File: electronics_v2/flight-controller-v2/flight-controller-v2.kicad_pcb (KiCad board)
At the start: 2 copper layers, 45 x 84 mm, 91 parts, among them J1 Conn_02x05_Odd_Even, J2 USB_B_Micro, J3 Conn_02x03_Odd_Even, J4 Conn_01x05, J5 Conn_01x06, J6 Conn_01x05, SW1 SW_Push, SW2 SW_Push, U1 LM1117-3.3, U2 STM32F411RETx, U3 ESP-12E, U4 CS49E, U5 LM393, U6 MPU-6050, U7 HMC5883L, U8 BMP280, Y1 8MHz

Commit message: update silkscreen and add tag for order number
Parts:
- moved JP1 1.50 mm to (155.0, 98.2)
- moved JP2 1.50 mm to (155.0, 95.5)
- moved JP3 1.50 mm to (155.0, 92.5)
- moved JP4 1.50 mm to (155.0, 89.8)
- moved JP5 1.50 mm to (155.0, 87.0)
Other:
- board text added: "GPIO0"
- board text added: "GPIO12"
- board text added: "GPIO2"
- board text added: "JLCJLCJLCJLC"
- board text added: "RXD0"
- board text added: "TXD0"
- board text removed: "MRX"
- board text removed: "MTX"
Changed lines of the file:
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@@
   )
   (footprint "Jumper:SolderJumper-2_P1.3mm_Open_TrianglePad1.0x1.5mm" (layer "B.Cu")
-    (at 156.5 95.5)
+    (at 155 95.5)
     (descr "SMD Solder Jumper, 1x1.5mm Triangular Pads, 0.3mm gap, open")
     (tags "solder jumper open")
@@
   )
   (footprint "Jumper:SolderJumper-2_P1.3mm_Open_TrianglePad1.0x1.5mm" (layer "B.Cu")
-    (at 156.5 87)
+    (at 155 87)
     (descr "SMD Solder Jumper, 1x1.5mm Triangular Pads, 0.3mm gap, open")
     (tags "solder jumper open")
@@
   )
   (footprint "Jumper:SolderJumper-2_P1.3mm_Open_TrianglePad1.0x1.5mm" (layer "B.Cu")
-    (at 156.5 89.75)
+    (at 155 89.75)
     (descr "SMD Solder Jumper, 1x1.5mm Triangular Pads, 0.3mm gap, open")
     (tags "solder jumper open")
@@
   )
   (footprint "Jumper:SolderJumper-2_P1.3mm_Open_TrianglePad1.0x1.5mm" (layer "B.Cu")
-    (at 156.5 92.5)
+    (at 155 92.5)
     (descr "SMD Solder Jumper, 1x1.5mm Triangular Pads, 0.3mm gap, open")
     (tags "solder jumper open")
@@
   )
   (footprint "Jumper:SolderJumper-2_P1.3mm_Open_TrianglePad1.0x1.5mm" (layer "B.Cu")
-    (at 156.5 98.25)
+    (at 155 98.25)
     (descr "SMD Solder Jumper, 1x1.5mm Triangular Pads, 0.3mm gap, open")
     (tags "solder jumper open")
@@
   (gr_arc (start 161.000001 85) (mid 161.292894 84.292894) (end 162 84.000001) (layer "Edge.Cuts") (width 0.1))
   (gr_arc (start 124 80) (mid 125.171573 77.171573) (end 128 76) (layer "Edge.Cuts") (width 0.1))
-  (gr_text "RST" (at 154.5 87) (layer "B.SilkS")
-    (effects (font (size 0.75 0.75) (thickness 0.15)) (justify left mirror))
+  (gr_text "RST" (at 156.75 87) (layer "B.SilkS")
+    (effects (font (size 0.75 0.75) (thickness 0.15)) (justify right mirror))
   )
-  (gr_text "UAV TVC Goose\nFlight Controller V2.0\nby Eryk Możdżeń\nJuly 2023" (at 158 81) (layer "B.SilkS")
+  (gr_text "UAV TVC Goose\nFlight Controller V2.0\nby Eryk Możdżeń\nJuly 2023" (at 156.75 81) (layer "B.SilkS")
     (effects (font (size 1 1) (thickness 0.15)) (justify left mirror))
   )
-  (gr_text "MRX" (at 154.5 98.25) (layer "B.SilkS")
+  (gr_text "GPIO0" (at 153.25 92.5) (layer "B.SilkS")
+    (effects (font (size 0.75 0.75) (thickness 0.15)) (justify left mirror))
+  )
+  (gr_text "RX" (at 156.75 98.25) (layer "B.SilkS")
+    (effects (font (size 0.75 0.75) (thickness 0.15)) (justify right mirror))
+  )
+  (gr_text "GPIO12" (at 153.25 87) (layer "B.SilkS")
     (effects (font (size 0.75 0.75) (thickness 0.15)) (justify left mirror))
   )
-  (gr_text "MTX" (at 154.5 95.5) (layer "B.SilkS")
+  (gr_text "TX" (at 156.75 95.5) (layer "B.SilkS")
+    (effects (font (size 0.75 0.75) (thickness 0.15)) (justify right mirror))
+  )
+  (gr_text "GPIO2" (at 153.25 89.75) (layer "B.SilkS")
     (effects (font (size 0.75 0.75) (thickness 0.15)) (justify left mirror))
   )
-  (gr_text "SWDIO" (at 154.5 92.5) (layer "B.SilkS")
+  (gr_text "SWDIO" (at 156.75 92.5) (layer "B.SilkS")
+    (effects (font (size 0.75 0.75) (thickness 0.15)) (justify right mirror))
+  )
+  (gr_text "TXD0" (at 153.25 98.25) (layer "B.SilkS")
     (effects (font (size 0.75 0.75) (thickness 0.15)) (justify left mirror))
   )
-  (gr_text "SWCLK" (at 154.5 89.75) (layer "B.SilkS")
+  (gr_text "SWCLK" (at 156.75 89.75) (layer "B.SilkS")
+    (effects (font (size 0.75 0.75) (thickness 0.15)) (justify right mirror))
+  )
+  (gr_text "RXD0" (at 153.25 95.5) (layer "B.SilkS")
     (effects (font (size 0.75 0.75) (thickness 0.15)) (justify left mirror))
   )
@@
     (effects (font (size 0.75 0.75) (thickness 0.15)))
   )
+  (gr_text "JLCJLCJLCJLC" (at 159 92.5 90) (layer "F.SilkS")
+    (effects (font (size 1 1) (thickness 0.2)))
+  )
   (gr_text "3V3" (at 165.75 113.5) (layer "F.SilkS")

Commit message: edge XT60 connector & INA226 I2C measurement
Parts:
- removed the C1 at (140.9, 110.0)
- removed the C6 at (140.9, 108.0)
- removed the D1 at (136.9, 113.0)
- removed the D2 at (136.9, 105.0)
- removed the J3 at (142.0, 143.7)
- removed the R1 at (137.4, 110.0)
- removed the R2 at (140.9, 112.0)
- removed the R3 at (137.4, 108.0)
- removed the R4 at (140.9, 106.0)
- added J6: Conn_02x03_Odd_Even, Connector_IDC:IDC-Header_2x03_P2.54mm_Vertical, F.Cu at (137.5, 146.5)
- moved R4 1.52 mm to (150.0, 140.0)
- moved R8 1.52 mm to (150.0, 142.0)
- moved G*** 0.50 mm to (155.1, 145.3)
- renumbered C2 to C1, C8 to C10, C9 to C11, C14 to C12, C10 to C13, C15 to C14, C11 to C15, C12 to C16, C7 to C17, C19 to C18, C26 to C19, C3 to C2, C27 to C20, C23 to C21, C24 to C22, C30 to C23, C31 to C24, C29 to C25, C25 to C26, C22 to C27, C4 to C3, C5 to C4, C20 to C5, C13 to C6, C21 to C7, C16 to C8, C17 to C9, D3 to D1, D4 to D2, D5 to D3, D6 to D4, J5 to J3, J6 to J5, R6 to R1, R15 to R10, R10 to R11, R9 to R12, R16 to R13, R11 to R14, R12 to R15, R23 to R16, R25 to R17, R24 to R18, R20 to R19, R5 to R2, R21 to R20, R22 to R21, R7 to R3, R13 to R4, R17 to R5, R18 to R6, R19 to R7, R14 to R9, U8 to U4, U4 to U5, U5 to U7, U7 to U8
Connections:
- net /sensors/I2C_SCL renamed /sensors/INT_I2C_SCL
- net /sensors/I2C_SDA renamed /sensors/INT_I2C_SDA
- J1 pad 10: /power/BATT_V_SENSE -> /power/EXT_I2C_SCL
- J1 pad 8: /power/BATT_I_SENSE -> /power/EXT_I2C_SDA
- R4 pad 2: /ucontroller/VLX_I2C3_SDA -> /power/EXT_I2C_SDA
- R8 pad 2: /ucontroller/VLX_I2C3_SCL -> /power/EXT_I2C_SCL
- U2 pad 24: /power/I_FILTER -> unconnected-(U2-Pad24)
- U2 pad 25: /power/V_FILTER -> unconnected-(U2-Pad25)
- U2 pad 40: /ucontroller/VLX_I2C3_SDA -> /power/EXT_I2C_SDA
- U2 pad 41: /ucontroller/VLX_I2C3_SCL -> /power/EXT_I2C_SCL
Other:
- board text removed: "ISENS"
- board text removed: "VSENS"

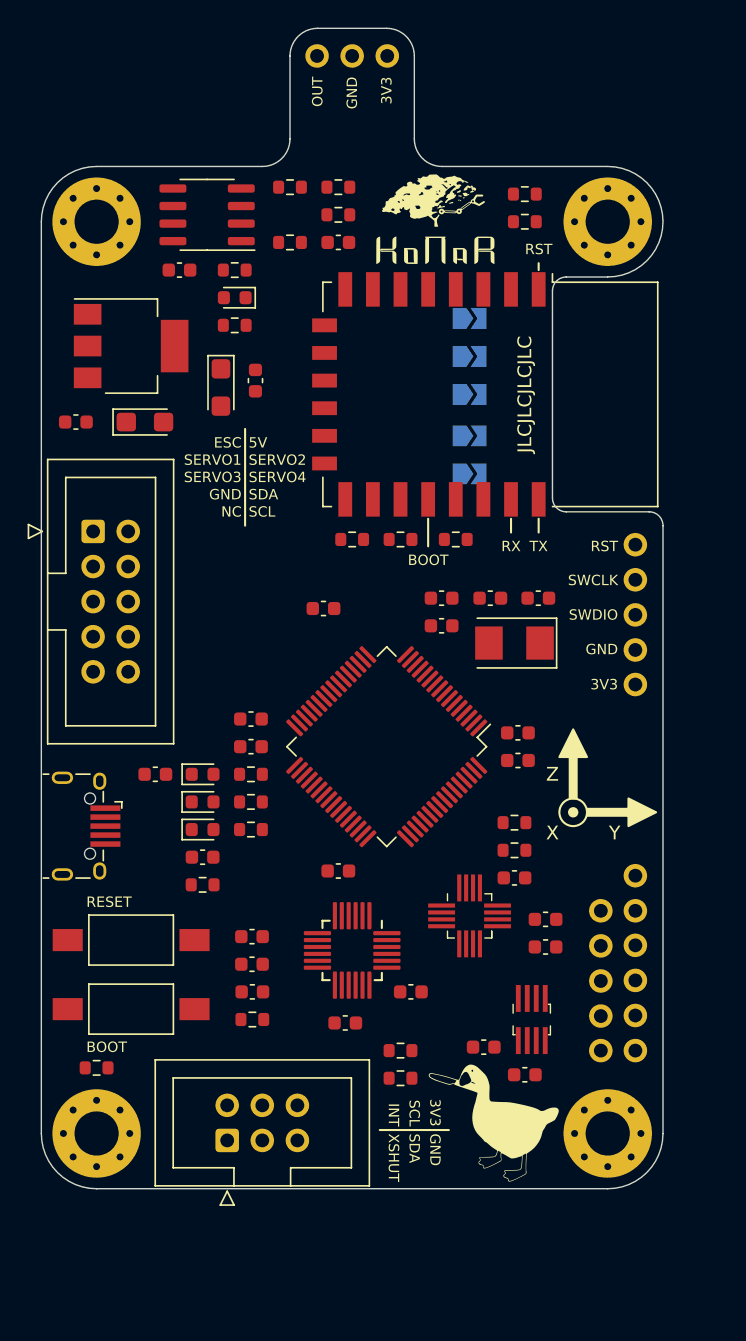
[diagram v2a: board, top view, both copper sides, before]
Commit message: move PLI to FC
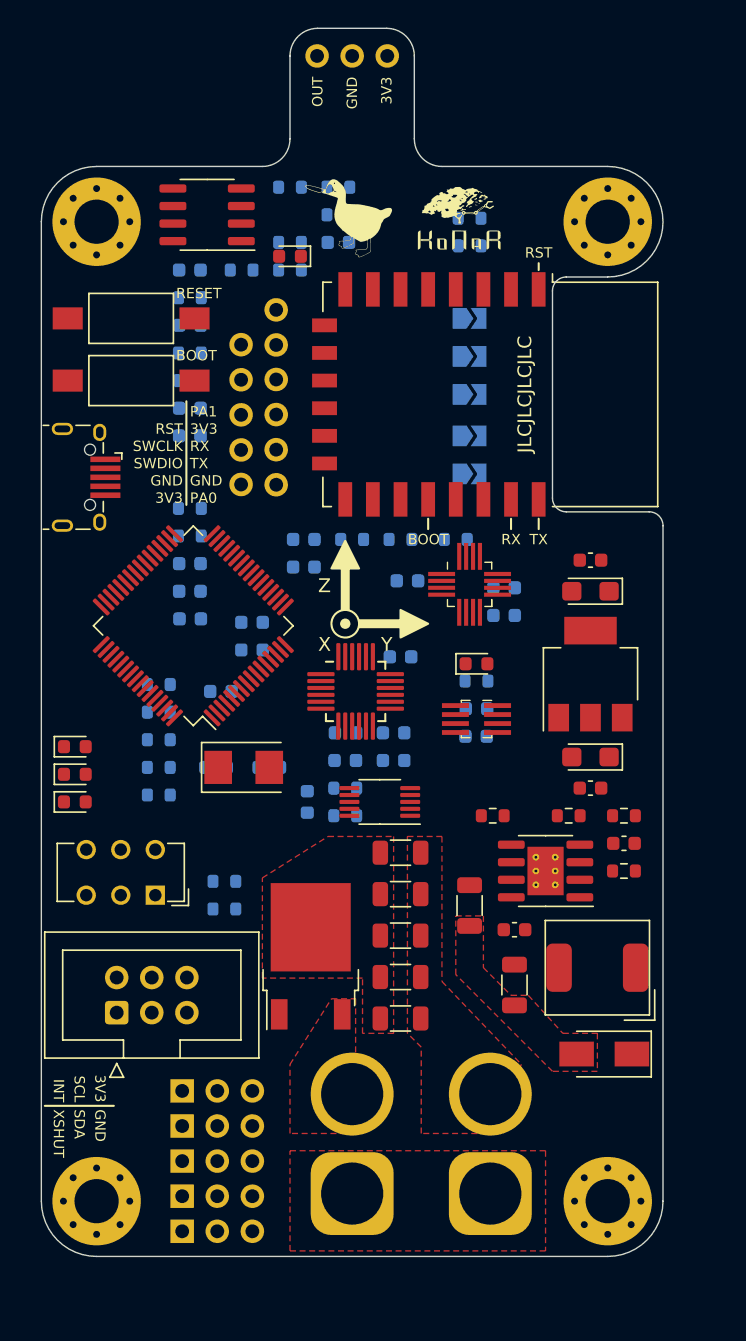
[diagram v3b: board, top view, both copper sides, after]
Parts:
- removed the G*** at (152.5, 80.5)
- removed the G*** at (155.1, 145.3)
- removed the G*** at (146.6, 108.2)
- added C10: 100n, Capacitor_SMD:C_0603_1608Metric, B.Cu at (146.0, 119.0)
- added C5: 10u/50V, Capacitor_SMD:C_1206_3216Metric, F.Cu at (155.0, 129.5)
- added C6: 100n, Capacitor_SMD:C_0603_1608Metric, F.Cu at (158.2, 131.2)
- added C7: 150p, Capacitor_SMD:C_0603_1608Metric, F.Cu at (166.2, 125.0)
- added C8: 22u/25V, Capacitor_SMD:C_1206_3216Metric, F.Cu at (158.2, 135.2)
- added C9: 100n, Capacitor_SMD:C_0603_1608Metric, B.Cu at (143.2, 122.0)
- added D1: RED, LED_SMD:LED_0603_1608Metric, F.Cu at (155.5, 112.0)
- added D2: SS34, Diode_SMD:D_SMA, F.Cu at (164.8, 140.2)
- added G***: LOGO, LOGO, F.Cu at (154.2, 80.2)
- added G***: LOGO, LOGO, F.Cu at (145.1, 79.8)
- added J2: Conn_01x03, Connector_PinHeader_2.54mm:PinHeader_1x03_P2.54mm_Vertical, B.Cu at (134.2, 153.1)
- added J3: Conn_01x03, Connector_PinHeader_2.54mm:PinHeader_1x03_P2.54mm_Vertical, B.Cu at (134.2, 150.5)
- added J4: Conn_01x03, Connector_PinHeader_2.54mm:PinHeader_1x03_P2.54mm_Vertical, B.Cu at (134.2, 148.0)
- added J6: Conn_01x03, Connector_PinHeader_2.54mm:PinHeader_1x03_P2.54mm_Vertical, B.Cu at (134.2, 142.9)
- added J7: Conn_01x02, Connector_AMASS:AMASS_XT60-F_1x02_P7.20mm_Vertical, B.Cu at (156.5, 150.3)
- added L1: 22u, Inductor_SMD:L_AVX_LMLP07A7, F.Cu at (164.2, 134.0)
- added Q1: IRFR5305, Package_TO_SOT_SMD:TO-252-2, F.Cu at (143.5, 133.2)
- added R1: 10k, Resistor_SMD:R_0603_1608Metric, B.Cu at (137.2, 129.8)
- added R10: 10m, Resistor_SMD:R_1206_3216Metric, F.Cu at (150.0, 137.7)
- added R11: 10, Resistor_SMD:R_0603_1608Metric, B.Cu at (146.0, 123.0)
- added R12: 10, Resistor_SMD:R_0603_1608Metric, B.Cu at (146.0, 121.0)
- added R13: 210k, Resistor_SMD:R_0603_1608Metric, F.Cu at (166.2, 123.0)
- added R14: 39k, Resistor_SMD:R_0603_1608Metric, F.Cu at (162.2, 123.0)
- added R2: 1k, Resistor_SMD:R_0603_1608Metric, B.Cu at (137.2, 127.8)
- added R3: 100k, Resistor_SMD:R_0603_1608Metric, F.Cu at (156.7, 123.0)
- added R4: 1k, Resistor_SMD:R_0603_1608Metric, B.Cu at (155.5, 113.2)
- added R5: 10m, Resistor_SMD:R_1206_3216Metric, F.Cu at (150.0, 125.7)
- added R6: 10m, Resistor_SMD:R_1206_3216Metric, F.Cu at (150.0, 128.7)
- added R7: 10m, Resistor_SMD:R_1206_3216Metric, F.Cu at (150.0, 131.7)
- added R8: 10m, Resistor_SMD:R_1206_3216Metric, F.Cu at (150.0, 134.7)
- added R9: 100k, Resistor_SMD:R_0603_1608Metric, F.Cu at (166.2, 127.0)
- added SW1: SW_Push_SPDT, Button_Switch_THT:SW_CuK_JS202011CQN_DPDT_Straight, F.Cu at (132.2, 128.8)
- added U2: MP1584, Package_SO:SOIC-8-1EP_3.9x4.9mm_P1.27mm_EP2.62x3.51mm_ThermalVias, F.Cu at (160.5, 127.0)
- added U3: INA226, Package_SO:VSSOP-10_3x3mm_P0.5mm, F.Cu at (148.5, 122.0)
- C11: renamed from C5; moved to B.Cu
- C12: renamed from C6; moved to B.Cu
- C13: renamed from C7; moved to B.Cu
- C14: renamed from C8; moved to B.Cu
- C15: renamed from C9; moved to B.Cu
- C16: renamed from C10; moved to B.Cu
- C17: renamed from C11; moved to B.Cu
- C18: renamed from C12; moved to B.Cu
- C19: renamed from C13; moved to B.Cu
- C20: renamed from C14; moved to B.Cu
- C21: renamed from C15; moved to B.Cu
- C22: renamed from C16; moved to B.Cu
- C23: renamed from C17; moved to B.Cu
- C24: renamed from C18; moved to B.Cu
- C25: renamed from C19; moved to B.Cu
- C26: renamed from C20; moved to B.Cu
- C27: renamed from C21; moved to B.Cu
- C28: renamed from C22; moved to B.Cu
- C29: renamed from C23; moved to B.Cu
- C30: renamed from C24; moved to B.Cu
- C31: renamed from C25; moved to B.Cu
- C32: renamed from C26; moved to B.Cu
- C33: renamed from C27; moved to B.Cu
- C34: renamed from C28; moved to B.Cu
- J1: value Conn_02x05_Odd_Even -> Conn_01x02; footprint Connector_IDC:IDC-Header_2x05_P2.54mm_Vertical -> Connector_AMASS:AMASS_XT60-M_1x02_P7.20mm_Vertical; moved to B.Cu
- J5: value Conn_01x05 -> Conn_01x03; footprint goose:tht_pin_01x05 -> Connector_PinHeader_2.54mm:PinHeader_1x03_P2.54mm_Vertical; moved to B.Cu
- R15: renamed from R1; moved to B.Cu
- R16: renamed from R2; moved to B.Cu
- R17: renamed from R3; moved to B.Cu
- R18: renamed from R4; moved to B.Cu
- R19: renamed from R5; moved to B.Cu
- R20: renamed from R6; moved to B.Cu
- R21: renamed from R7; moved to B.Cu
- R22: renamed from R8; moved to B.Cu
- R23: renamed from R9; moved to B.Cu
- R24: renamed from R10; moved to B.Cu
- R25: renamed from R11; moved to B.Cu
- R26: renamed from R12; moved to B.Cu
- R27: renamed from R13; moved to B.Cu
- R28: renamed from R14; moved to B.Cu
- R29: renamed from R15; moved to B.Cu
- R30: renamed from R16; moved to B.Cu
- R31: renamed from R17; moved to B.Cu
- R32: renamed from R18; moved to B.Cu
- R33: renamed from R19; moved to B.Cu
- R34: renamed from R20; moved to B.Cu
- R35: renamed from R21; moved to B.Cu
- moved R15 52.2 mm to (134.8, 89.5)
- moved J1 51.5 mm to (146.5, 150.3), turned to 90 degrees
- moved J9 48.5 mm to (141.0, 86.4)
- moved R17 46.5 mm to (134.8, 91.5), turned to 0 degrees
- moved C1 45.7 mm to (163.8, 121.0)
- moved SW3 45.5 mm to (130.5, 91.5)
- moved SW2 45.0 mm to (130.5, 87.0)
- moved R16 42.5 mm to (134.8, 85.5)
- moved C14 42.5 mm to (134.8, 93.5), turned to 180 degrees
- moved R18 42.1 mm to (134.8, 100.8)
- moved R22 42.1 mm to (134.8, 102.8)
- moved U1 40.9 mm to (163.8, 112.8), turned to 90 degrees
- moved C2 40.4 mm to (163.8, 118.8), turned to 180 degrees
- moved C12 38.5 mm to (134.8, 87.5)
- moved J10 32.0 mm to (138.5, 99.0)
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- renumbered D1 to D3, D2 to D4, D3 to D5, D4 to D6, J4 to J10, J6 to J11, J2 to J8, J3 to J9, SW1 to SW2, SW2 to SW3, U8 to U10, U2 to U4, U3 to U5, U4 to U6, U5 to U7, U6 to U8, U7 to U9
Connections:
- net /sensors/INT_I2C_SCL renamed /power/INT_I2C_SCL
- net /sensors/INT_I2C_SDA renamed /power/INT_I2C_SDA
- J1 pad 1: /power/PWM_THROTTLE -> GND
- J1 pad 2: +5V -> /power/BATTERY_IN
- J11 pad 3: /power/EXT_I2C_SDA -> /sensors/EXT_I2C3_SDA
- J11 pad 4: /power/EXT_I2C_SCL -> /sensors/EXT_I2C3_SCL
- J5 pad 1: /ucontroller/SPI3_MISO -> /power/PWM_SERVO4
- J5 pad 2: /ucontroller/SPI3_MOSI -> +5V
- J5 pad 3: /ucontroller/SPI3_SCK -> GND
- R18 pad 2: /power/EXT_I2C_SDA -> /ucontroller/EXT_I2C3_SDA
- R22 pad 2: /power/EXT_I2C_SCL -> /ucontroller/EXT_I2C3_SCL
- U4 pad 40: /power/EXT_I2C_SDA -> /ucontroller/EXT_I2C3_SDA
- U4 pad 41: /power/EXT_I2C_SCL -> /ucontroller/EXT_I2C3_SCL
- U4 pad 42: /power/PWM_THROTTLE -> /power/PWM_ESC
- U4 pad 51: /ucontroller/SPI3_SCK -> unconnected-(U4-Pad51)
- U4 pad 52: /ucontroller/SPI3_MISO -> unconnected-(U4-Pad52)
- U4 pad 53: /ucontroller/SPI3_MOSI -> unconnected-(U4-Pad53)
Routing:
- added copper zone on F.Cu, net /power/BATTERY_IN
- added copper zone on F.Cu, net /power/SUPPLY
- added copper zone on F.Cu, net GND
- added copper zone on F.Cu, net VBUS
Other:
- board size 45 x 84 mm -> 45 x 88.9 mm
- board text added: "PA0"
- board text added: "PA1"
- board text added: "PWM"
- board text added: "S1"
- board text added: "S2"
- board text added: "S3"
- board text added: "S4"
- board text removed: "NC"
- board text removed: "SERVO1"
- board text removed: "SERVO2"
- board text removed: "SERVO3"
- board text removed: "SERVO4"

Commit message: movemounting hole by 0.1mm
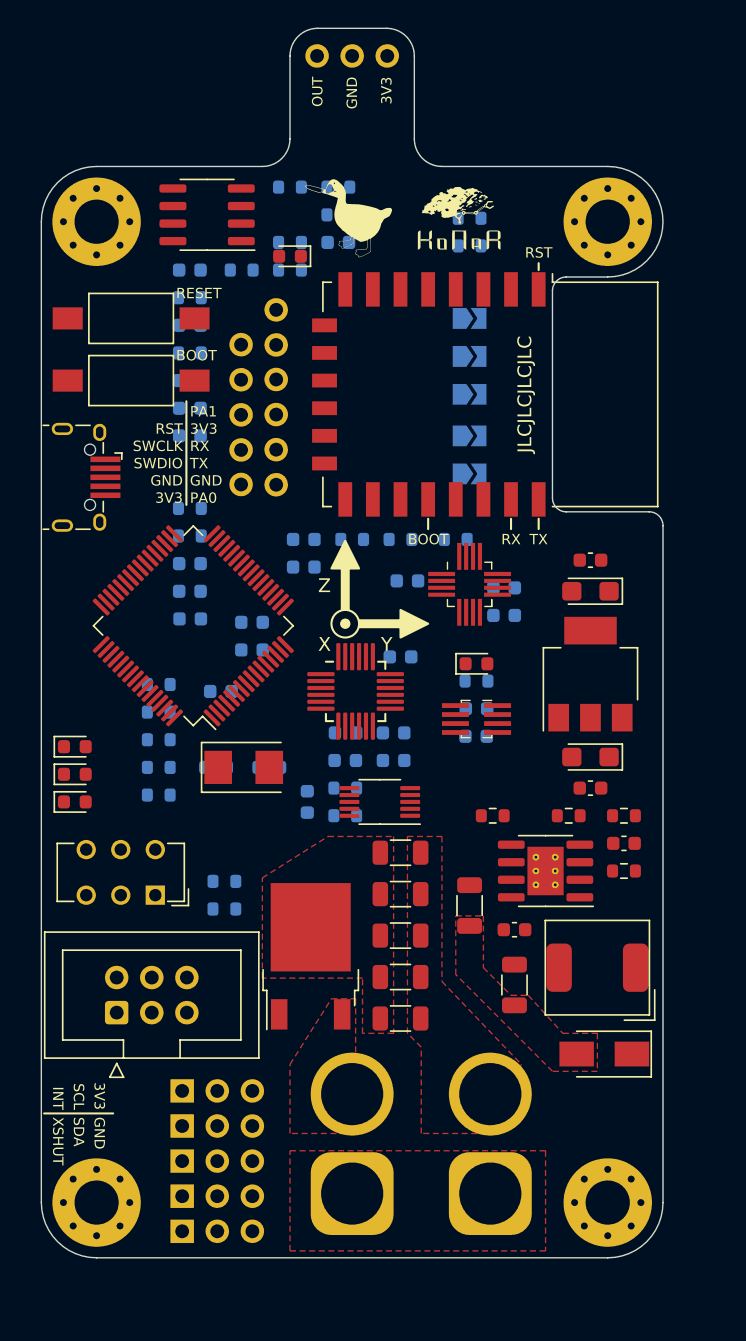
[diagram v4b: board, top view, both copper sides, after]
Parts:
- moved H3 0.10 mm to (128.0, 151.0)
- moved H4 0.10 mm to (165.0, 151.0)
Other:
- board size 45 x 88.9 mm -> 45 x 89 mm

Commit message: fix route names
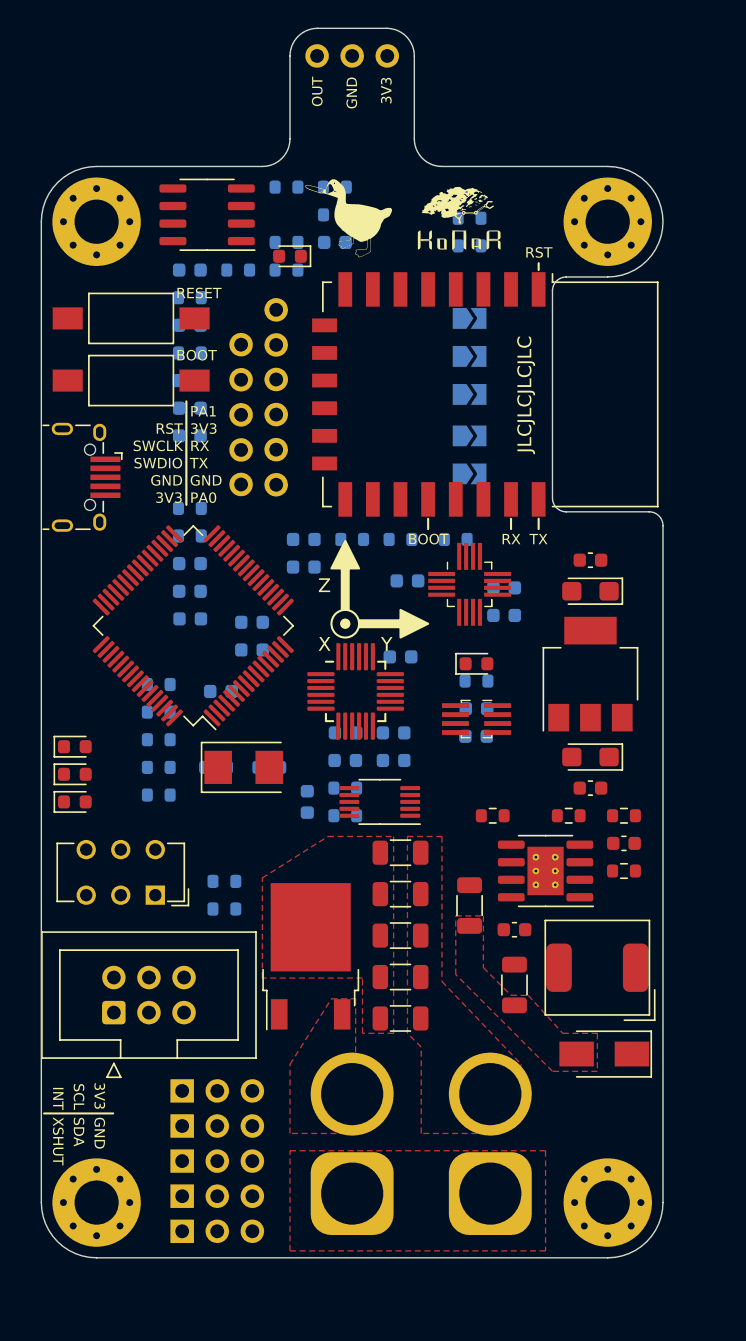
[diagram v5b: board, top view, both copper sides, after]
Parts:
- removed J11: Conn_02x03_Odd_Even, Connector_IDC:IDC-Header_2x03_P2.54mm_Vertical
- added J12: Conn_02x03_Odd_Even, Connector_IDC:IDC-Header_2x03_P2.54mm_Vertical, F.Cu at (129.2, 137.2)
- moved C24 0.25 mm to (145.2, 81.5)
- moved R30 0.25 mm to (145.2, 79.5)
- moved R31 0.25 mm to (145.2, 77.5)
- moved R32 0.25 mm to (141.8, 77.5)
- moved R33 0.25 mm to (138.2, 83.5)
- moved R34 0.25 mm to (141.8, 81.5)
- moved R35 0.25 mm to (141.8, 83.5)
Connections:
- net /ucontroller/EXT_I2C3_SCL renamed /sensors/VLX_SCL
- net /ucontroller/EXT_I2C3_SDA renamed /sensors/VLX_SDA
- C10 pad 2: +3V3 -> +3.3V
- C33 pad 1: +3V3 -> +3.3V
- D6 pad 2: +3V3 -> +3.3V
- R30 pad 1: +3V3 -> +3.3V
- R34 pad 2: +3V3 -> +3.3V
- R4 pad 1: +3V3 -> +3.3V
- U3 pad 6: +3V3 -> +3.3V
- U4 pad 2: /ucontroller/VLX_XSHUT -> /sensors/VLX_XSHUT
- U4 pad 3: /ucontroller/VLX_INT -> /sensors/VLX_INT
- U7 pad 1: +3V3 -> +3.3V
- U9 pad 8: +3V3 -> +3.3V
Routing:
- added copper zone on In2.Cu, net +3.3V
- added copper zone on In1.Cu, net GND
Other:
- copper layers 2 -> 4
